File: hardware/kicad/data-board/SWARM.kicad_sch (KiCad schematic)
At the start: 6 parts, among them U12 Swarm_M138

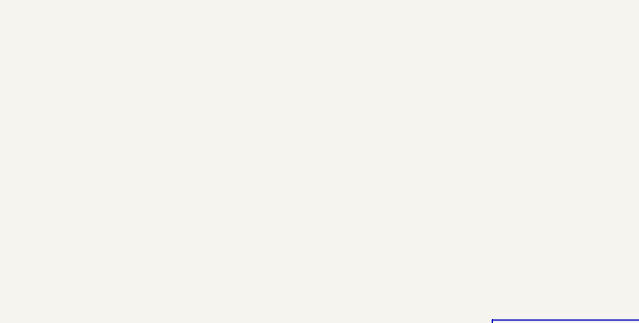
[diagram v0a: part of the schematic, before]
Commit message: change i2c pin interface
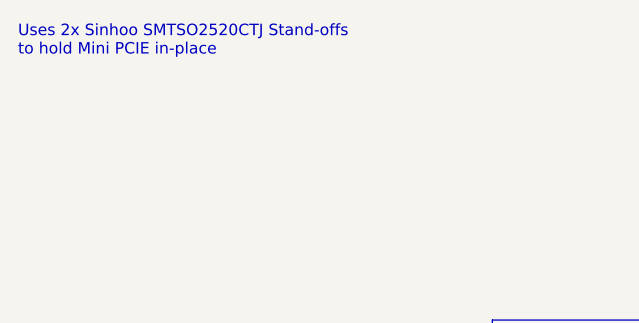
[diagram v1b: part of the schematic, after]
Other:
- note added: "Uses 2x Sinhoo SMTSO2520CTJ Stand-offs to hold Mini PCIE in-place"
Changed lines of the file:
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@@
     (effects (font (size 2.0066 2.0066)) (justify left bottom))
+  )
+  (text "Uses 2x Sinhoo SMTSO2520CTJ Stand-offs\nto hold Mini PCIE in-place"
+    (at 14.605 19.05 0)
+    (effects (font (size 1.27 1.27)) (justify left bottom))
   )
   (text "Ceramic capacitors rated for 16V or greater, X5R or better"
